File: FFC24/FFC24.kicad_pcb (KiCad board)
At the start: 4 copper layers, 7 parts, among them J1 XF2M-1015-1A-mod, J2 XF2M-1015-1A-mod, J3 xf2m-2415-1a-mod, J4 XF2M-1015-1A-mod, J5 XF2M-1015-1A-mod, J6 XF2M-1015-1A-mod, J7 XF2M-1015-1A-mod

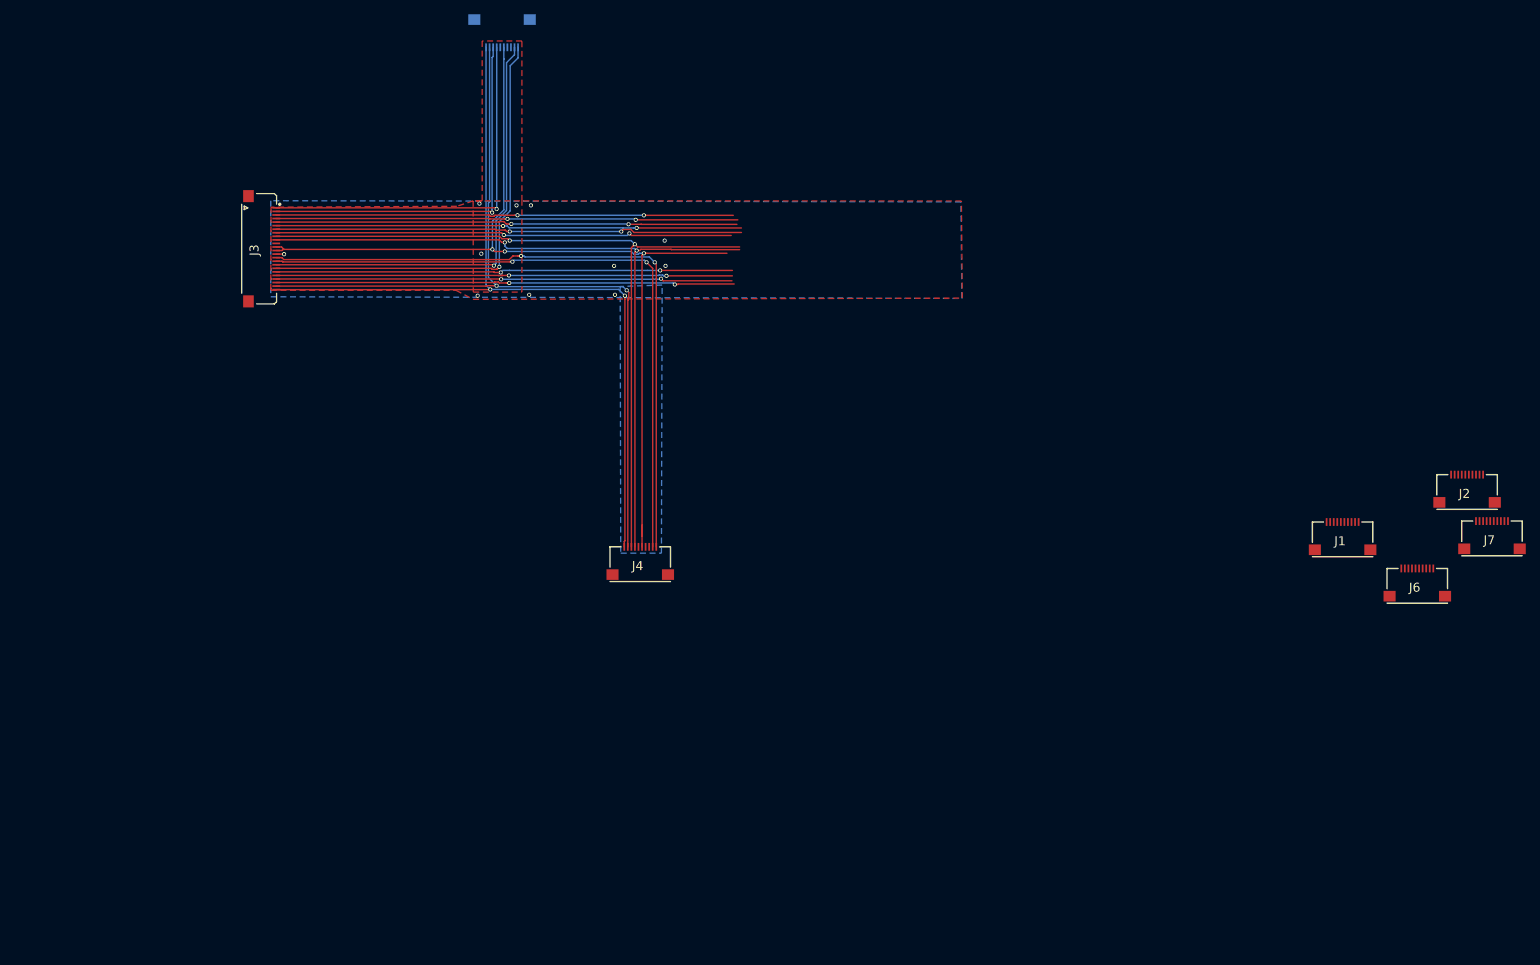
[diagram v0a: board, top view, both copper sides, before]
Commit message: starting to route flex cable
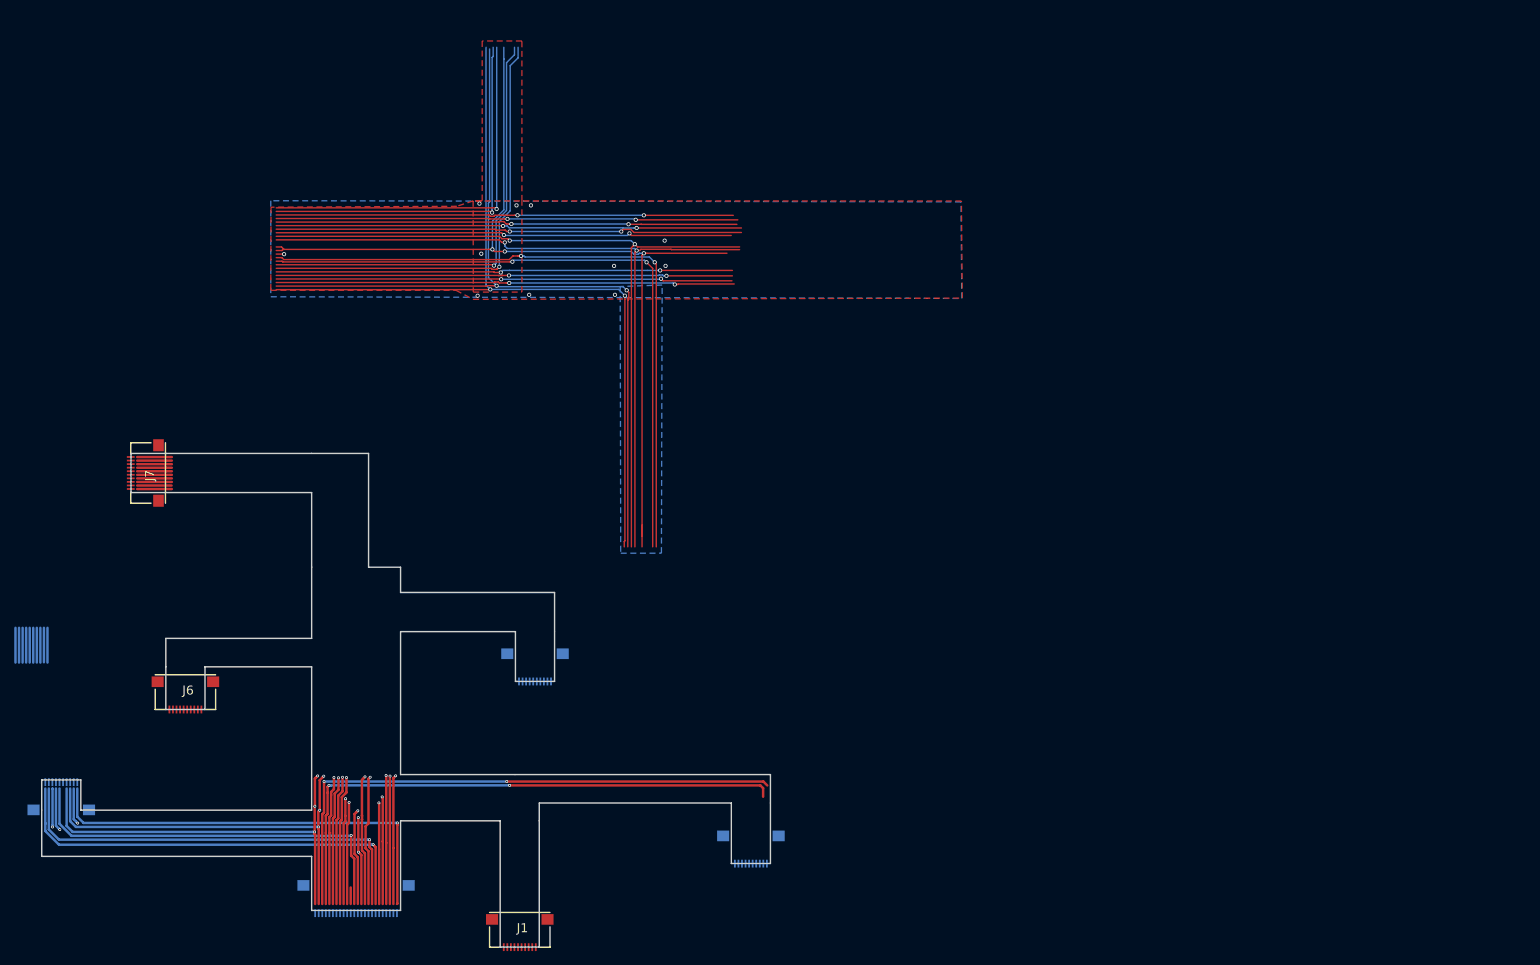
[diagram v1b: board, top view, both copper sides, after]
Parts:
- J2, J3, J4: moved to B.Cu
- moved J7 191.5 mm to (52.1, 122.0), turned to 90 degrees
- moved J6 174.3 mm to (59.8, 155.2), turned to 180 degrees
- moved J1 130.2 mm to (106.8, 188.6), turned to 180 degrees
- moved J5 120.5 mm to (42.3, 165.4), turned to 180 degrees
- moved J2 114.6 mm to (139.2, 176.9)
- moved J3 94.1 mm to (83.7, 183.8), turned to 0 degrees
- moved J4 24.0 mm to (108.9, 151.3)
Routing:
- net COIL6_P: track 64.4 -> 144.3 mm, vias 2 -> 4
- net 3V3: track 137.0 -> 216.8 mm, vias 3 -> 5
- net COIL6_N: track 65.0 -> 144.3 mm, vias 2 -> 4
- net COIL3_P: track 63.5 -> 134.7 mm, vias 1 -> 2
- net BATT_P: track 119.0 -> 189.5 mm, vias 2 -> 3
- net COIL3_N: track 62.5 -> 133.0 mm, vias 1 -> 2
- net SCL2: track 53.8 -> 122.2 mm, vias 1 -> 4
- net SDA2: track 53.7 -> 121.6 mm, vias 1 -> 4
- net GND: track 1.11 -> 44.4 mm, vias 11 -> 15
- net BATT_N: track 119.8 -> 152.7 mm, vias 2 -> 4
- net COIL4_N: track 92.7 -> 111.0 mm, vias 2 -> 3
- net COIL4_P: track 94.0 -> 112.2 mm, vias 2 -> 3
- net BURN1: track 65.8 -> 84.0 mm, vias 2 -> 3
- net BURN2: track 64.4 -> 82.5 mm, vias 2 -> 3
- net COIL1_N: track 64.2 -> 82.3 mm, vias 2 -> 3
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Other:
- board outline added: 102.5 x 69.4 mm
- net class Default: clearance 0.127 -> 0.15; trace_width 0.127 -> 0.35; via_dia 0.5842 -> 0.4; via_drill 0.3556 -> 0.2
- rule trace_clearance: 0.127 -> 0.15
- rule trace_min: 0.1 -> 0.35
- rule via_min_size: 0.5 -> 0.4

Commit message: roughed out the layout
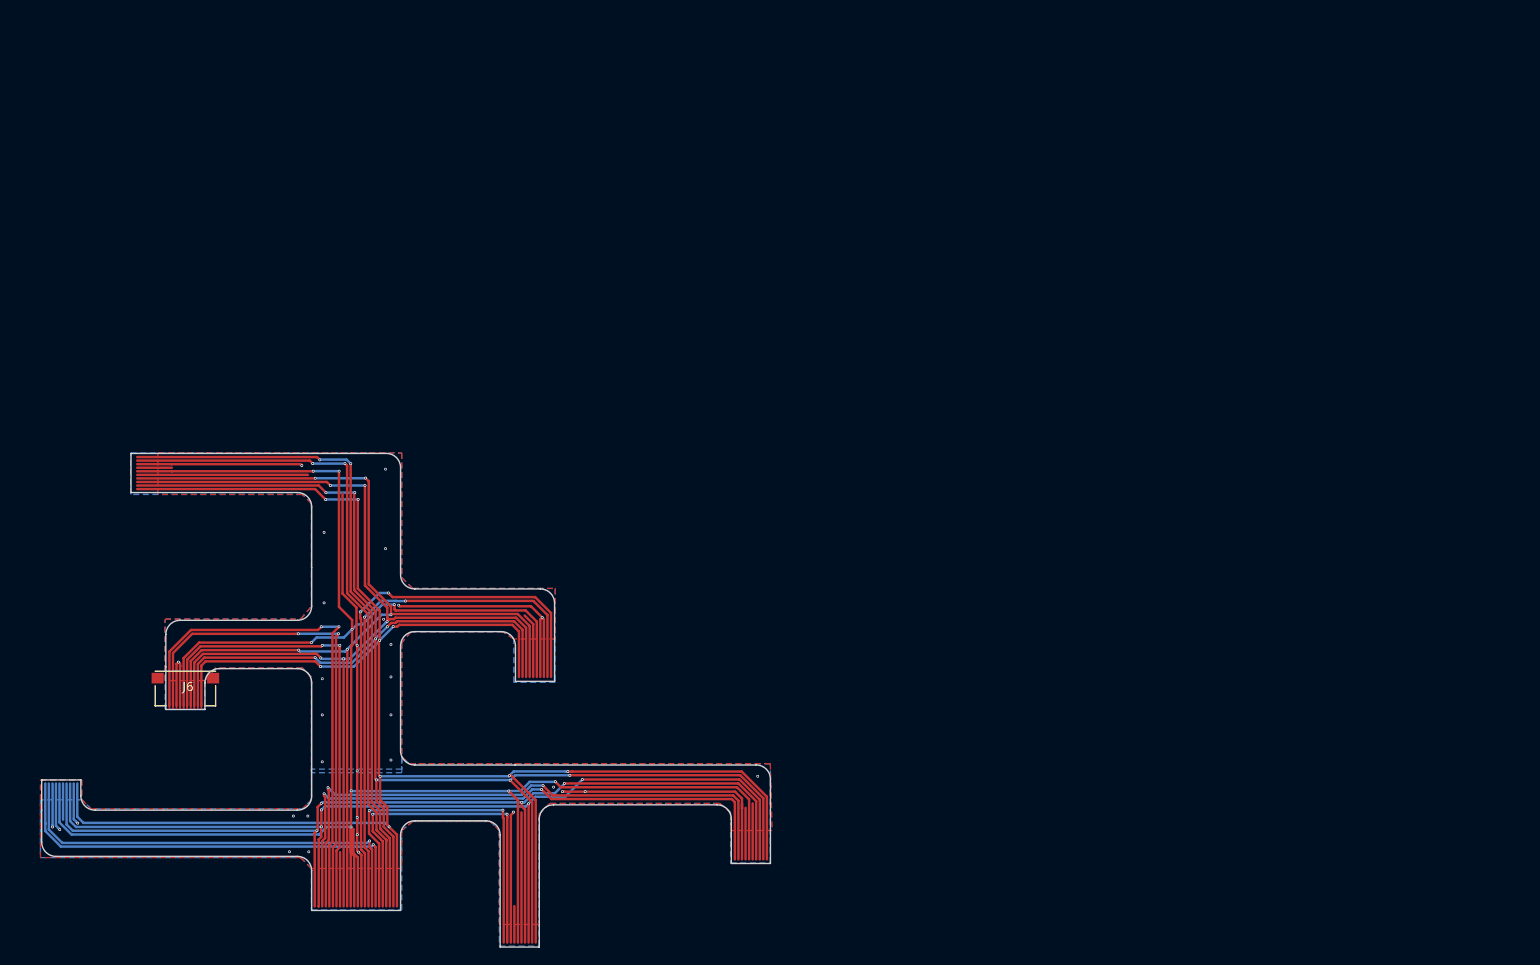
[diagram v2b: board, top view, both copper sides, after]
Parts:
- removed J1, J2, J4, J5, J7: XF2M-1015-1A-mod, custom-footprints:XF2M-1015-1A
- removed J3: xf2m-2415-1a-mod, custom-footprints:XF2M-2415-1A
- moved J6 0.51 mm to (59.8, 154.7)
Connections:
- J6 pad 3: SDA2 -> SDA1
- J6 pad 4: SCL2 -> SCL1
- J6 pad 5: Net-(J6-Pad5) -> BURN1
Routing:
- net GND: track 44.4 -> 216.3 mm, vias 15 -> 32
- net 3V3: track 216.8 -> 321.0 mm, vias 5 -> 9
- net BATT_P: track 189.5 -> 290.6 mm, vias 3 -> 9
- net BATT_N: track 152.7 -> 247.9 mm, vias 4 -> 9
- net BURN2: track 82.5 -> 7.62 mm, vias 3 -> 0
- net COIL3_P: track 134.7 -> 62.7 mm, vias 2 -> 1
- net COIL3_N: track 133.0 -> 61.8 mm, vias 2 -> 1
- net COIL6_P: track 144.3 -> 83.4 mm, vias 4 -> 2
- net COIL6_N: track 144.3 -> 84.7 mm, vias 4 -> 2
- net Net-(J5-Pad5): track 9.77 -> 47.4 mm
- net COIL4_N: track 111.0 -> 77.1 mm, vias 3 -> 2
- net COIL4_P: track 112.2 -> 79.8 mm, vias 3 -> 2
- net SCL1: track 122.3 -> 153.7 mm, vias 3 -> 5
- net COIL2_N: track 79.4 -> 50.5 mm, vias 3 -> 2
- net SDA1: track 123.4 -> 150.9 mm, vias 3 -> 5
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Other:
- outline, holes or cut-outs redrawn

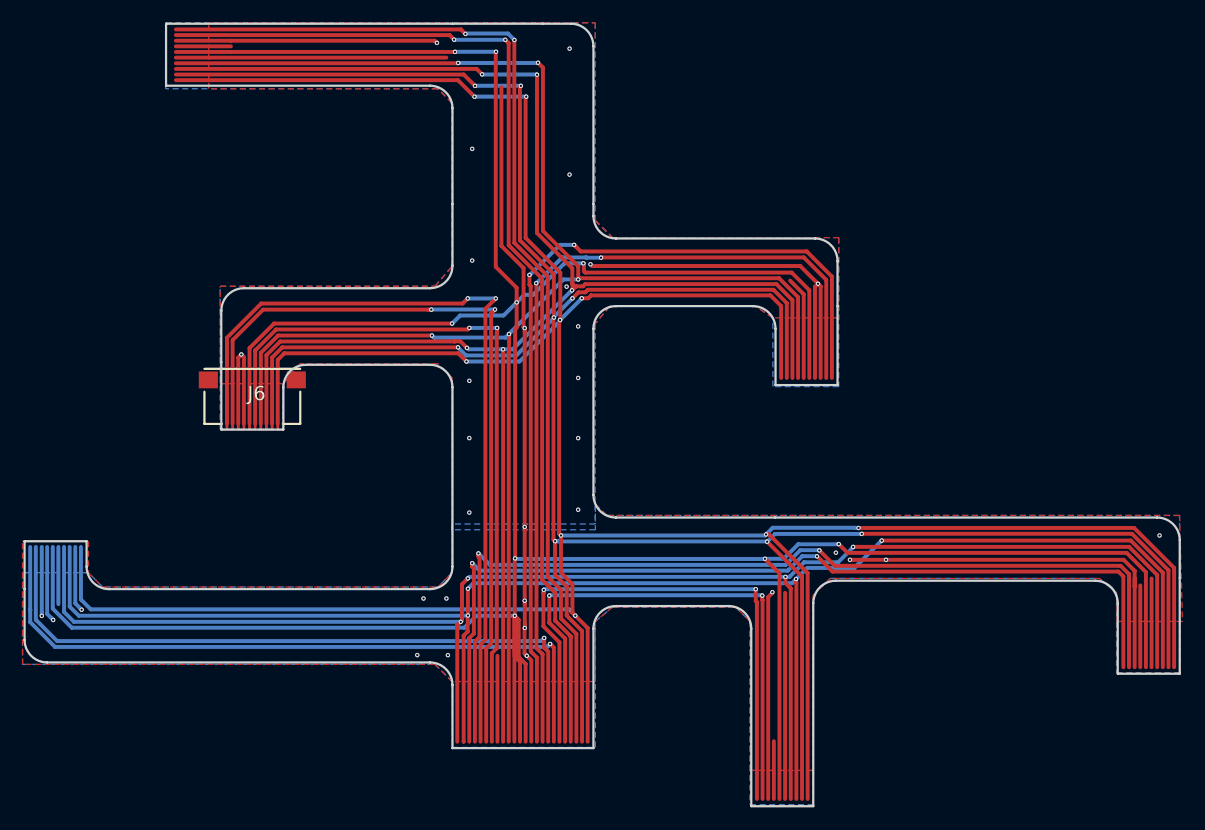
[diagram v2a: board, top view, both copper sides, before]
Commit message: FFC tweaks
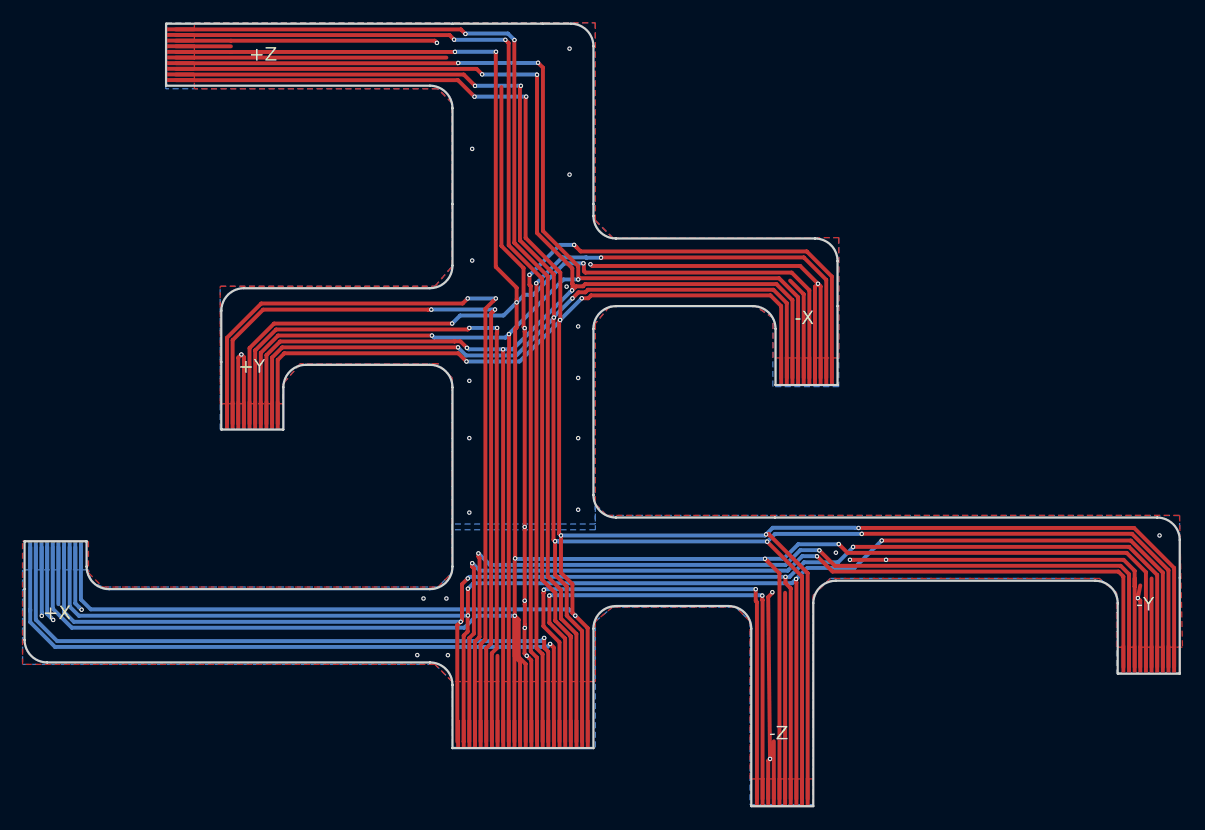
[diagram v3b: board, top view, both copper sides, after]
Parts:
- added J1: XF2M-1015-1A-mod, custom-footprints:FFC-10pin, F.Cu at (106.8, 187.3)
- added J2: XF2M-1015-1A-mod, custom-footprints:FFC-10pin, F.Cu at (139.2, 175.6)
- added J3: xf2m-2415-1a-mod, custom-footprints:FFC-24pin, F.Cu at (83.8, 182.2)
- added J4: XF2M-1015-1A-mod, custom-footprints:FFC-10pin, F.Cu at (108.9, 150.0)
- added J5: XF2M-1015-1A-mod, custom-footprints:FFC-10pin, B.Cu at (42.3, 166.3)
- added J7: XF2M-1015-1A-mod, custom-footprints:FFC-10pin, F.Cu at (53.4, 122.0)
- J6: footprint custom-footprints:XF2M-1015-1A -> custom-footprints:FFC-10pin
- moved J6 0.74 mm to (59.8, 153.9)
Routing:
- net Net-(J5-Pad5): track 47.4 -> 5.08 mm
- net Net-(J7-Pad5): track 0.00 -> 24.0 mm
- net Net-(J1-Pad5): track 0.00 -> 18.3 mm
- net GND: track 216.3 -> 216.4 mm, vias 32 -> 34
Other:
- board text added: "+X"
- board text added: "+Y"
- board text added: "+Z"
- board text added: "-X"
- board text added: "-Y"
- board text added: "-Z"

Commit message: FFC clean up
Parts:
- J5: moved to F.Cu
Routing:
- net BATT_N: track 247.9 -> 291.2 mm, vias 9 -> 10
- net 3V3: track 321.0 -> 295.0 mm, vias 9 -> 10
- net Net-(J7-Pad5): track 24.0 -> 4.30 mm
- net GND: track 216.4 -> 205.9 mm, vias 34 -> 38
- net SCL2: track 147.6 -> 148.9 mm
- net COIL1_P: track 95.0 -> 93.9 mm
- net COIL1_N: track 94.1 -> 93.1 mm
- net BATT_P: track 290.6 -> 289.5 mm, vias 9 -> 10
- net SDA1: track 150.9 -> 149.9 mm
- net SCL1: track 153.7 -> 152.7 mm
- net BURN2: track 7.62 -> 6.69 mm
- net COIL6_N: track 84.7 -> 84.0 mm
- net COIL5_N: track 70.5 -> 69.8 mm
- net BURN1: track 65.7 -> 65.0 mm
- net COIL5_P: track 72.8 -> 72.1 mm
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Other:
- copper layers 4 -> 2

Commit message: first cable order
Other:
- board text added: "1"
- board text added: "cablev00"
